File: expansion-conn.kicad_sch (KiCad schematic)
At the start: 7 parts, among them J7 Plug_Samtec_ERM8_2x40_ERM8-04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

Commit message: [#100765] Update subsheets
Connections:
- net 12V_CONN renamed V_{cc}
- net PCIE2_CLKREQ renamed PCIe_{x2}.~{CLK_REQ}
- net PCIE2_CLK_N renamed PCIe_{x2}.CLK_N
- net PCIE2_CLK_P renamed PCIe_{x2}.CLK_P
- net PCIE2_RST renamed PCIe_{x2}.~{RST}
- net PCIE2_RX0_N renamed PCIe_{x2}.RX0_N
- net PCIE2_RX0_P renamed PCIe_{x2}.RX0_P
- net PCIE2_RX1_N renamed PCIe_{x2}.RX1_N
- net PCIE2_RX1_P renamed PCIe_{x2}.RX1_P
- net PCIE2_TX0_N renamed PCIe_{x2}.TX0_N
- net PCIE2_TX0_P renamed PCIe_{x2}.TX0_P
- net PCIE2_TX1_N renamed PCIe_{x2}.TX1_N
- net PCIE2_TX1_P renamed PCIe_{x2}.TX1_P
- net USB1_D_N: no longer names the net of J7.41
- net USB1_D_P: no longer names the net of J7.43

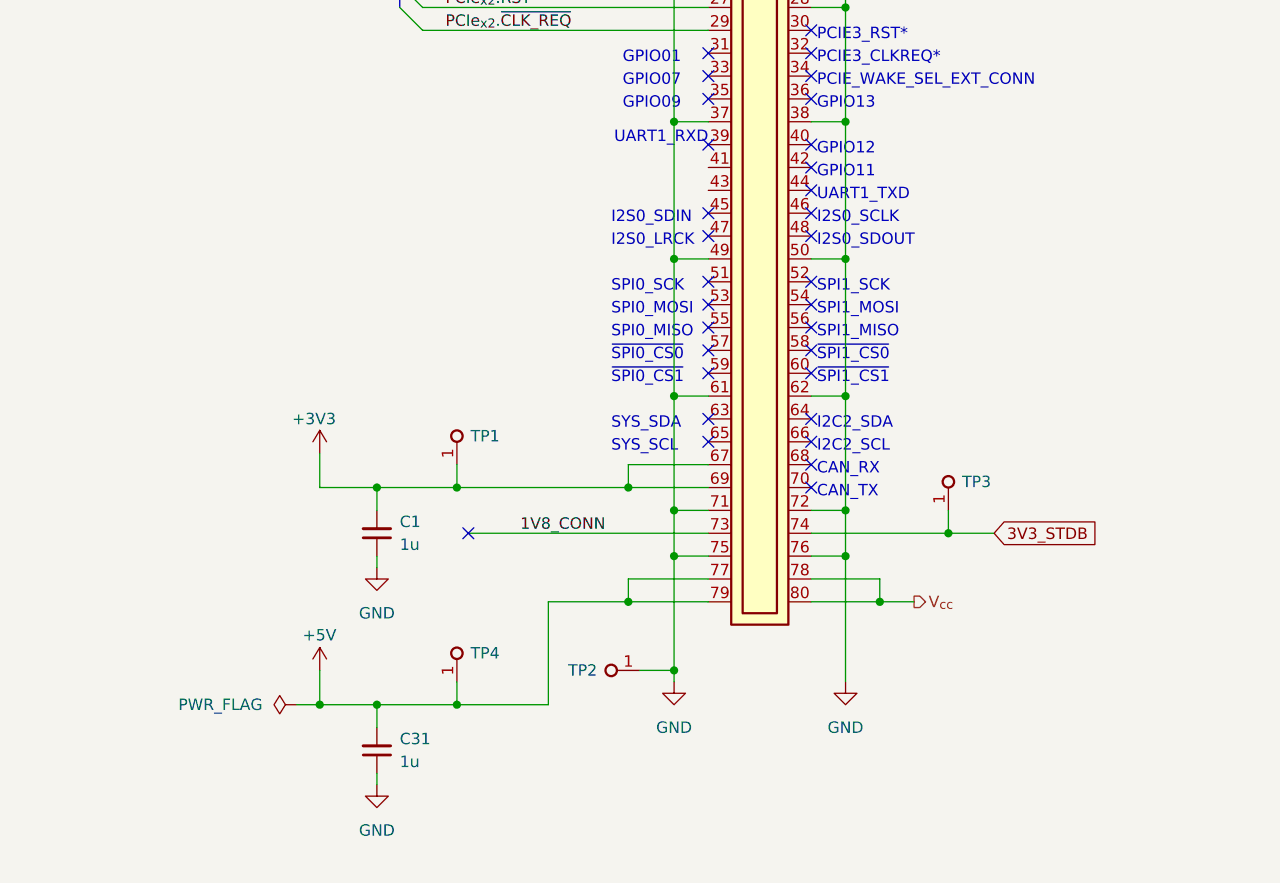
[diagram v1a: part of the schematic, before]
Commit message: [#100765] Add lane config tables
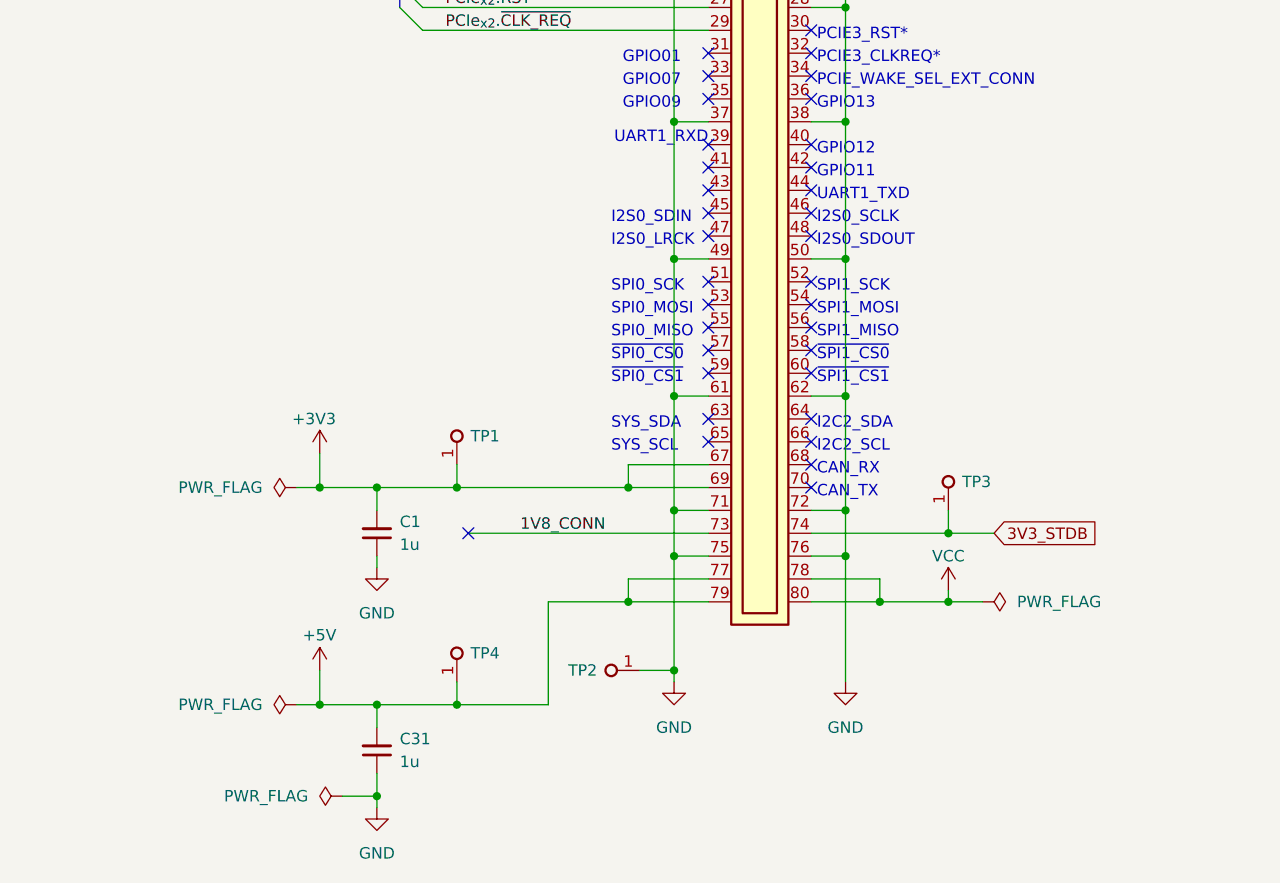
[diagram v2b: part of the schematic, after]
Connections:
- net V_{cc} renamed VCC
- no-connect marks 38 -> 40

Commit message: [#100765] Update schematic
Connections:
- net POWER_EN: now also J7.31
- net +3V3 renamed +3V3_JOB
- no-connect marks 40 -> 39
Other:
- note removed: "GPIO01"
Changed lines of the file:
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@@
-		)
-	)
-	(text "GPIO01"
-		(exclude_from_sim no)
-		(at 135.255 81.28 0)
-		(effects
-			(font
-				(size 1.27 1.27)
-			)
-			(justify left bottom)
 		)
 	)
@@
 	)
 	(junction
-		(at 101.6 128.27)
-		(diameter 0)
-		(color 0 0 0 0)
-	)
-	(junction
 		(at 140.97 102.87)
 		(diameter 0)
@@
 	(no_connect
 		(at 156.21 64.77)
-	)
-	(no_connect
-		(at 144.78 80.01)
 	)
 	(no_connect
@@
 	(wire
 		(pts
+			(xy 132.08 80.01) (xy 144.78 80.01)
+		)
+		(stroke
+			(width 0)
+			(type default)
+		)
+	)
+	(wire
+		(pts
 			(xy 140.97 135.89) (xy 144.78 135.89)
 		)
@@
 	(wire
 		(pts
-			(xy 101.6 124.46) (xy 101.6 128.27)
-		)
-		(stroke
-			(width 0)
-			(type default)
-		)
-	)
-	(wire
-		(pts
 			(xy 107.95 128.27) (xy 107.95 130.81)
 		)
@@
 	(wire
 		(pts
-			(xy 99.06 128.27) (xy 101.6 128.27)
-		)
-		(stroke
-			(width 0)
-			(type default)
-		)
-	)
-	(wire
-		(pts
 			(xy 107.95 162.56) (xy 107.95 163.83)
 		)
@@
 	(wire
 		(pts
-			(xy 101.6 128.27) (xy 107.95 128.27)
+			(xy 99.06 128.27) (xy 107.95 128.27)
 		)
 		(stroke
@@
 			(width 0)
 			(type default)
+		)
+	)
+	(label "+3V3_JOB"
+		(at 121.92 128.27 0)
+		(effects
+			(font
+				(size 1.27 1.27)
+			)
+			(justify left bottom)
 		)
 	)
@@
 	(hierarchical_label "POWER_EN"
 		(shape output)
-		(at 231.14 85.09 0)
-		(effects
-			(font
-				(size 1.27 1.27)
-			)
-			(justify left)
+		(at 132.08 80.01 180)
+		(effects
+			(font
+				(size 1.27 1.27)
+			)
+			(justify right)
 		)
 	)
@@
 					(unit 1)
 				)
-			)
-		)
-	)
-	(symbol
-		(lib_id "antmicropower:+3V3")
-		(at 101.6 124.46 0)
-		(unit 1)
-		(body_style 1)
-		(exclude_from_sim no)
-		(in_bom yes)
-		(on_board yes)
-		(in_pos_files yes)
-		(dnp no)
-		(property "Reference" "#PWR01"
-			(at 101.6 128.27 0)
-			(hide yes)
-			(show_name no)
-			(do_not_autoplace no)
-			(effects
-				(font
-					(size 1.27 1.27)
-				)
-			)
-		)
-		(property "Value" "+3V3"
-			(at 100.965 120.65 0)
-			(show_name no)
-			(do_not_autoplace no)
-			(effects
-				(font
-					(size 1.27 1.27)
-				)
-			)
-		)
-		(property "Footprint" ""
-			(at 101.6 124.46 0)
-			(hide yes)
-			(show_name no)
-			(do_not_autoplace no)
-			(effects
-				(font
-					(size 1.27 1.27)
-				)
-			)
-		)
-		(property "Datasheet" ""
-			(at 101.6 124.46 0)
-			(hide yes)
-			(show_name no)
-			(do_not_autoplace no)
-			(effects
-				(font
-					(size 1.27 1.27)
-				)
-			)
-		)
-		(property "Description" ""
-			(at 101.6 124.46 0)
-			(show_name no)
-			(do_not_autoplace no)
-			(effects
-				(font
-					(size 1.27 1.27)
-				)
-			)
-		)
-		(property "Author" "Antmicro"
-			(at 116.84 127 0)
-			(hide yes)
-			(show_name no)
-			(do_not_autoplace no)
-			(effects
-				(font
-					(size 1.27 1.27)
-					(thickness 0.15)
-				)
-				(justify left bottom)
-			)
-		)
-		(property "License" "Apache-2.0"
-			(at 116.84 129.54 0)
-			(hide yes)
-			(show_name no)
-			(do_not_autoplace no)
-			(effects
-				(font
-					(size 1.27 1.27)
-					(thickness 0.15)
-				)
-				(justify left bottom)
-			)
-		)
-		(pin "1"
-		)
-		(instances
-			(project "antmicro-jetson-orin-baseboard-pcie-switch-expansion-hw"
-				(path "/9f8272ef-d62d-4578-9094-a2852fcd4bf4/e2953c32-de4d-49db-967a-cd128c95e407"
-					(reference "#PWR01")
-					(unit 1)
-				)

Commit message: [#100765] Add LLC to I2C of the PCIe switch
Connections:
- net SDA: now reaches J7.63
- net SCL: now reaches J7.65
- no-connect marks 39 -> 37
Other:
- note removed: "SYS_SCL"
- note removed: "SYS_SDA"
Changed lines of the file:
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@@
-		)
-	)
-	(text "SYS_SCL"
-		(exclude_from_sim no)
-		(at 133.985 124.46 0)
-		(effects
-			(font
-				(size 1.27 1.27)
-			)
-			(justify left bottom)
 		)
 	)
@@
 		)
 	)
-	(text "SYS_SDA"
-		(exclude_from_sim no)
-		(at 133.985 121.92 0)
-		(effects
-			(font
-				(size 1.27 1.27)
-			)
-			(justify left bottom)
-		)
-	)
 	(text "PCIE_WAKE_SEL_EXT_CONN"
 		(exclude_from_sim no)
@@
 	)
 	(no_connect
-		(at 144.78 123.19)
-	)
-	(no_connect
 		(at 118.11 133.35)
 	)
@@
 	(no_connect
 		(at 156.21 107.95)
-	)
-	(no_connect
-		(at 144.78 120.65)
 	)
 	(no_connect
@@
 	)
 	(bus_entry
+		(at 130.81 118.11)
+		(size 2.54 2.54)
+		(stroke
+			(width 0)
+			(type default)
+		)
+	)
+	(bus_entry
 		(at 110.49 49.53)
 		(size 2.54 2.54)
@@
 	)
 	(bus_entry
+		(at 130.81 120.65)
+		(size 2.54 2.54)
+		(stroke
+			(width 0)
+			(type default)
+		)
+	)
+	(bus_entry
 		(at 113.03 62.23)
 		(size -2.54 -2.54)
@@
 		)
 	)
+	(wire
+		(pts
+			(xy 133.35 123.19) (xy 144.78 123.19)
+		)
+		(stroke
+			(width 0)
+			(type default)
+		)
+	)
 	(bus
 		(pts
@@
 	(wire
 		(pts
+			(xy 133.35 120.65) (xy 144.78 120.65)
+		)
+		(stroke
+			(width 0)
+			(type default)
+		)
+	)
+	(wire
+		(pts
 			(xy 156.21 138.43) (xy 163.83 138.43)
 		)
@@
 		)
 	)
+	(bus
+		(pts
+			(xy 130.81 116.84) (xy 129.54 116.84)
+		)
+		(stroke
+			(width 0)
+			(type default)
+		)
+	)
 	(wire
 		(pts
@@
 		(pts
 			(xy 160.02 130.81) (xy 160.02 135.89)
+		)
+		(stroke
+			(width 0)
+			(type default)
+		)
+	)
+	(bus
+		(pts
+			(xy 130.81 116.84) (xy 130.81 120.65)
 		)
 		(stroke
@@
 		)
 	)
+	(label "SDA"
+		(at 134.62 120.65 0)
+		(effects
+			(font
+				(size 1.27 1.27)
+			)
+			(justify left bottom)
+		)
+	)
 	(label "PCIe_{x2}.RX0_P"
 		(at 170.18 57.15 0)
@@
 			)
 			(justify right bottom)
+		)
+	)
+	(label "SCL"
+		(at 134.62 123.19 0)
+		(effects
+			(font
+				(size 1.27 1.27)
+			)
+			(justify left bottom)
 		)
 	)
@@
 		(effects
 			(font
+				(size 1.27 1.27)
+			)
+			(justify right)
+		)
+	)
+	(hierarchical_label "{I_{2}C}"
+		(shape bidirectional)
+		(at 129.54 116.84 180)
+		(effects
+			(font

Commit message: [#100765] Update schematic
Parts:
- removed C1, C31: C_1u_0402, antmicro-footprints:C_0402_1005Metric, symbol antmicroCapacitors0402:C_1u_0402
- removed TP1, TP3: TP_0.75mm_SMD, antmicro-footprints:TP_SMD_0.75mm, symbol antmicroTestPoints:TP_0.75mm_SMD
- added C56, C57: C_1u_0402, antmicro-footprints:C_0402_1005Metric, symbol antmicroCapacitors0402:C_1u_0402
- added TP18, TP19, TP20, TP21, TP22, TP23, TP24: TP_0.75mm_SMD, antmicro-footprints:TP_SMD_0.75mm, symbol antmicroTestPoints:TP_0.75mm_SMD
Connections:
- net +3V3_JOB: now also C56.2, TP23.1
- net +5V: now also C57.2
- net 3V3_STDB: now also TP24.1
- net GND: now also C56.1, C57.1
- net SEL: now reaches J7.40
- net at J7.51: now also TP18.1
- net at J7.53: now also TP19.1
- net at J7.55: now also TP20.1
- net at J7.57: now also TP21.1
- net at J7.59: now also TP22.1
- no-connect marks 37 -> 31

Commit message: [#100765] Change sheet format to A3, update schematic
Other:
- company: (none) -> Antmicro
- title: (none) -> antmicro-jetson-orin-baseboard-pcie-switch-expansion-hw
- moved on the sheet: C56, C57, J7, TP18, TP19, TP2, TP20, TP21, TP22, TP23, TP24, TP4

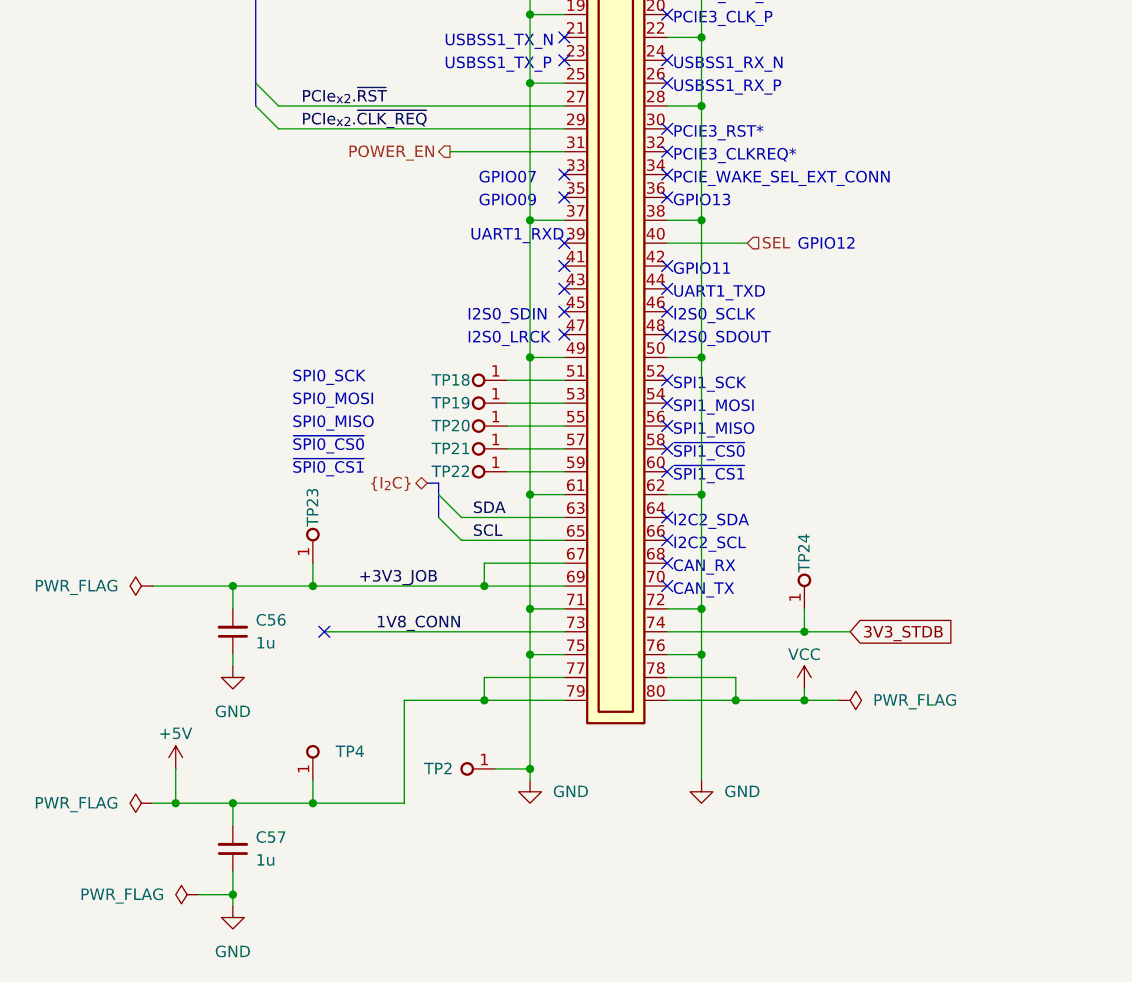
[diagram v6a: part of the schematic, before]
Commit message: [#100765] WIP: Apply review changes
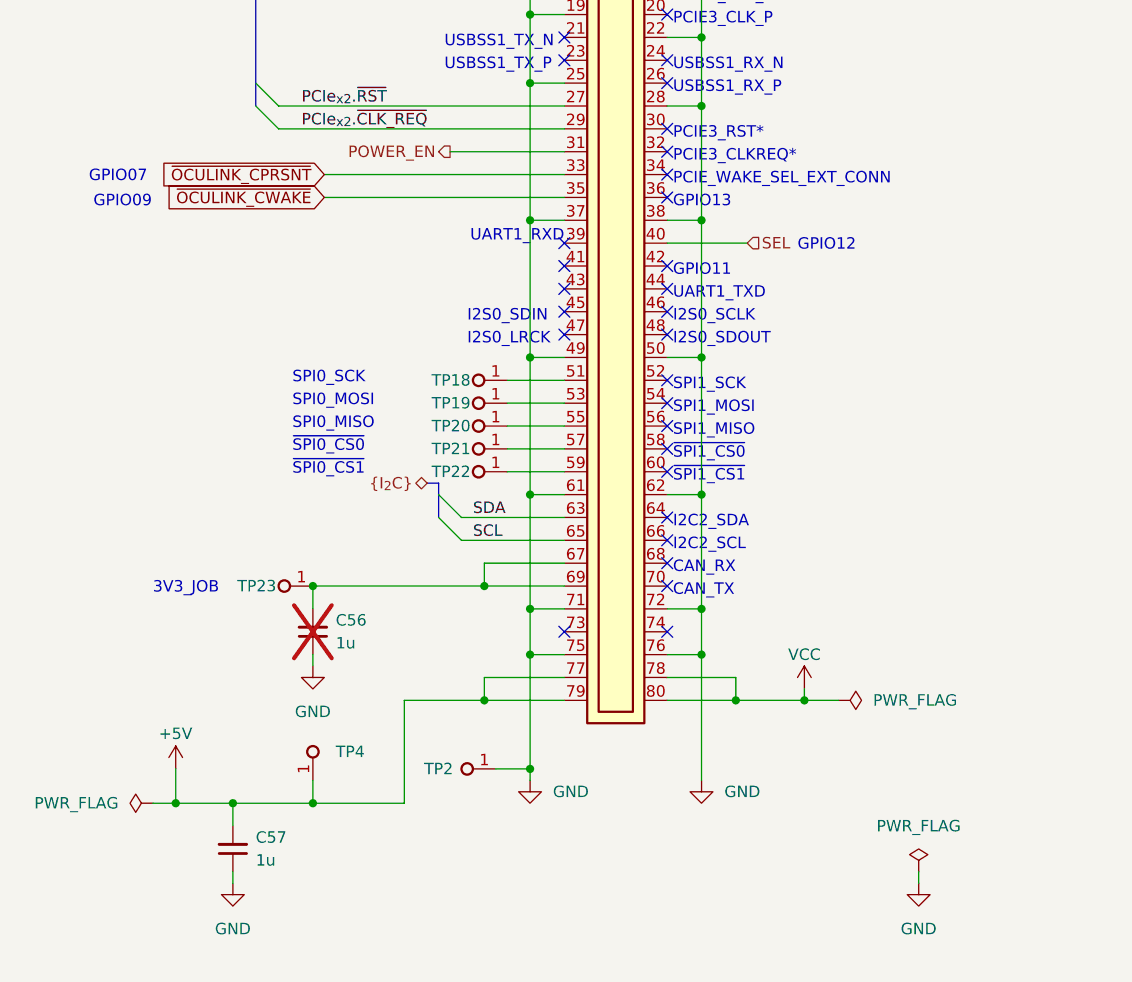
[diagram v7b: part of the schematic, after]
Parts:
- removed TP24: TP_0.75mm_SMD, antmicro-footprints:TP_SMD_0.75mm, symbol antmicroTestPoints:TP_0.75mm_SMD
- C56: now not fitted
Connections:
- net ~{OCULINK_CPRSNT}: now reaches J7.33
- net ~{OCULINK_CWAKE}: now reaches J7.35
- net +3V3_JOB: no longer names the net of C56.2, J7.67, J7.69, TP23.1
- net 1V8_CONN: no longer names the net of J7.73
- net 3V3_STDB: no longer names the net of J7.74
- no-connect marks 31 -> 30
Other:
- note added: "3V3_JOB"
- moved on the sheet: TP23

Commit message: [#100765] Apply fixes from review
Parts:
- added R117, R118: R_0R_0402, antmicro-footprints:R_0402_1005Metric, symbol antmicroResistors0402:R_0R_0402
- added TP42, TP43: TP_0.75mm_SMD, antmicro-footprints:TP_SMD_0.75mm, symbol antmicroTestPoints:TP_0.75mm_SMD
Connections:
- net SCL: now also TP42.1
- net SDA: now also TP43.1
- net ~{OCULINK_CPRSNT}: now also R117.1; no longer J7.33
- net ~{OCULINK_CWAKE}: now also R118.1; no longer J7.35
- new net: J7.33, R117.2
- new net: J7.35, R118.2
